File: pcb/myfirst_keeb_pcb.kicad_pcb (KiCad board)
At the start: 2 copper layers, 155 parts, among them SW1 SW_Push, SW2 SW_Push, SW3 Rotary_Encoder_Switch, U1 SRV05-4, U2 MCP1700-3302E_SOT23, U3 STM32F410CBTx

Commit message: remove switch for rst, use same switch as BOOT0 - add jtag for swd
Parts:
- removed SW2: SW_Push, Button_Switch_SMD:SW_SPST_B3S-1000
- added J1: Conn_ARM_JTAG_SWD_10, Connector_PinHeader_1.27mm:PinHeader_2x05_P1.27mm_Vertical_SMD, B.Cu at (157.4, 118.8)
- added Q1: DTC123J, Package_TO_SOT_SMD:SOT-23, B.Cu at (163.0, 128.0)
- moved C2 181.9 mm to (215.6, 125.7), turned to 90 degrees
- moved C6 96.4 mm to (200.5, 131.6)
- moved SW1 57.4 mm to (154.4, 128.0), turned to 180 degrees
- moved C7 39.3 mm to (198.6, 123.1), turned to 90 degrees
- moved C5 8.69 mm to (196.8, 128.5)
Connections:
- net Net-(R3-Pad2) renamed BOOT0
- C5 pad 2: GND -> NRST
- U3 pad 7: Net-(C5-Pad1) -> NRST
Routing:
- net SWDIO: track 0.00 -> 78.7 mm, vias 0 -> 2
- net SWDCLK: track 0.00 -> 57.4 mm, vias 0 -> 2
- net NRST: track 0.00 -> 51.1 mm, vias 0 -> 4
- net BOOT0: track 13.6 -> 61.9 mm, vias 0 -> 2
- net Net-(C5-Pad1): track 55.8 -> 36.6 mm, vias 2 -> 0
- net GND: track 708.4 -> 698.1 mm, vias 3 -> 4
- net D+: track 505.8 -> 503.6 mm
- net D-: track 495.7 -> 493.6 mm
- net +3V3: track 395.9 -> 396.1 mm, vias 4 -> 6

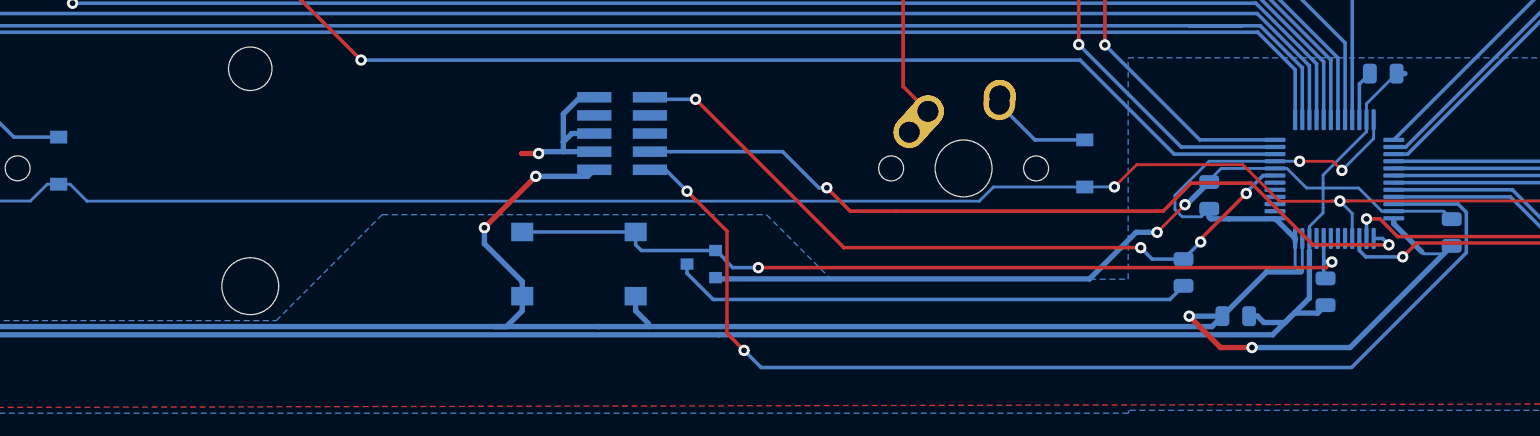
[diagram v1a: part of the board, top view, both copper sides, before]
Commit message: moved boot button to directly under spacebar
- easy push
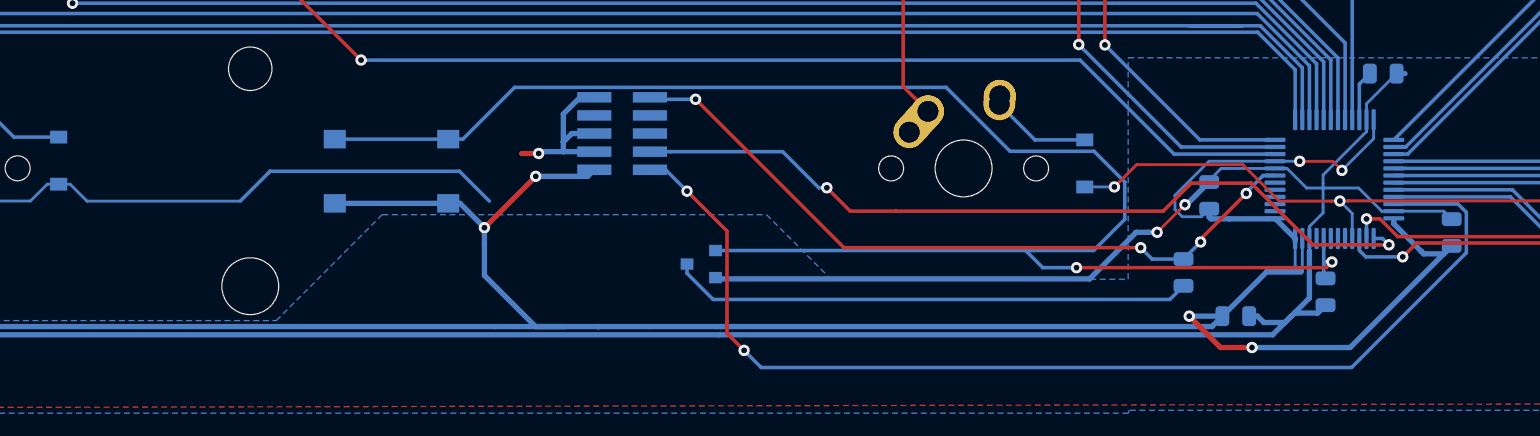
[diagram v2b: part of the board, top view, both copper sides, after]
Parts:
- moved SW1 14.7 mm to (141.3, 121.4)
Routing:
- net BOOT0: track 61.9 -> 117.4 mm
- net ROW4: track 313.8 -> 273.3 mm
- net +3V3: track 396.1 -> 406.4 mm

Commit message: shorten and made data bus lengths similar
- fix row trace unconnected
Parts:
- moved U1 7.50 mm to (116.7, 32.5)
- moved R2 6.98 mm to (111.1, 32.5)
- moved R1 6.12 mm to (111.1, 34.9)
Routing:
- net D+: track 503.6 -> 169.8 mm, vias 0 -> 7
- net D-: track 493.6 -> 169.8 mm, vias 0 -> 7
- net ROW4: track 273.3 -> 318.6 mm
- net GND: track 698.1 -> 705.4 mm
- net Net-(R2-Pad2): track 18.6 -> 11.9 mm
- net Net-(R1-Pad2): track 18.5 -> 12.2 mm
- net VCC: track 40.0 -> 38.5 mm

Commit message: add M2 mounting holes & rounded board cut-out
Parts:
- added H1: MountingHole, MountingHole:MountingHole_2.2mm_M2, F.Cu at (150.4, 31.1)
- added H2: MountingHole, MountingHole:MountingHole_2.2mm_M2, F.Cu at (255.1, 31.1)
- added H3: MountingHole, MountingHole:MountingHole_2.2mm_M2, F.Cu at (359.9, 31.1)
- added H4: MountingHole, MountingHole:MountingHole_2.2mm_M2, F.Cu at (359.9, 135.3)
- added H5: MountingHole, MountingHole:MountingHole_2.2mm_M2, F.Cu at (255.2, 135.3)
- added H6: MountingHole, MountingHole:MountingHole_2.2mm_M2, F.Cu at (150.4, 135.4)
- added H7: MountingHole, MountingHole:MountingHole_2.2mm_M2, F.Cu at (45.6, 135.3)
- added H8: MountingHole, MountingHole:MountingHole_2.2mm_M2, F.Cu at (45.6, 31.1)
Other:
- board outline added: 320.9 x 111.1 mm
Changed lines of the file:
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@@
   (general
     (thickness 1.6)
-    (drawings 2000)
+    (drawings 2008)
     (tracks 1199)
     (zones 0)
-    (modules 156)
+    (modules 164)
     (nets 122)
   )
@@
     (add_net VCC)
   )
+  (module MountingHole:MountingHole_2.2mm_M2 (layer F.Cu)
+    (at 45.62 31.11)
+    (descr "Mounting Hole 2.2mm, no annular, M2")
+    (tags "mounting hole 2.2mm no annular m2")
+    (attr virtual)
+    (fp_text reference H8 (at 0 -3.2) (layer F.SilkS)
+      (effects (font (size 1 1) (thickness 0.15)))
+    )
+    (fp_text value MountingHole (at 0 3.2) (layer F.Fab)
+      (effects (font (size 1 1) (thickness 0.15)))
+    )
+    (fp_text user %R (at 0.3 0) (layer F.Fab)
+      (effects (font (size 1 1) (thickness 0.15)))
+    )
+    (fp_circle (center 0 0) (end 2.2 0) (layer Cmts.User) (width 0.15))
+    (fp_circle (center 0 0) (end 2.45 0) (layer F.CrtYd) (width 0.05))
+    (pad 1 np_thru_hole circle (at 0 0) (size 2.2 2.2) (drill 2.2) (layers *.Cu *.Mask))
+  )
+  (module MountingHole:MountingHole_2.2mm_M2 (layer F.Cu)
+    (at 45.6 135.35)
+    (descr "Mounting Hole 2.2mm, no annular, M2")
+    (tags "mounting hole 2.2mm no annular m2")
+    (attr virtual)
+    (fp_text reference H7 (at 0 -3.2) (layer F.SilkS)
+      (effects (font (size 1 1) (thickness 0.15)))
+    )
+    (fp_text value MountingHole (at 0 3.2) (layer F.Fab)
+      (effects (font (size 1 1) (thickness 0.15)))
+    )
+    (fp_circle (center 0 0) (end 2.45 0) (layer F.CrtYd) (width 0.05))
+    (fp_circle (center 0 0) (end 2.2 0) (layer Cmts.User) (width 0.15))
+    (fp_text user %R (at 0.3 0) (layer F.Fab)
+      (effects (font (size 1 1) (thickness 0.15)))
+    )
+    (pad 1 np_thru_hole circle (at 0 0) (size 2.2 2.2) (drill 2.2) (layers *.Cu *.Mask))
+  )
+  (module MountingHole:MountingHole_2.2mm_M2 (layer F.Cu)
+    (at 150.37 135.36)
+    (descr "Mounting Hole 2.2mm, no annular, M2")
+    (tags "mounting hole 2.2mm no annular m2")
+    (attr virtual)
+    (fp_text reference H6 (at 0 -3.2) (layer F.SilkS)
+      (effects (font (size 1 1) (thickness 0.15)))
+    )
+    (fp_text value MountingHole (at 0 3.2) (layer F.Fab)
+      (effects (font (size 1 1) (thickness 0.15)))
+    )
+    (fp_circle (center 0 0) (end 2.45 0) (layer F.CrtYd) (width 0.05))
+    (fp_circle (center 0 0) (end 2.2 0) (layer Cmts.User) (width 0.15))
+    (fp_text user %R (at 0.3 0) (layer F.Fab)
+      (effects (font (size 1 1) (thickness 0.15)))
+    )
+    (pad 1 np_thru_hole circle (at 0 0) (size 2.2 2.2) (drill 2.2) (layers *.Cu *.Mask))
+  )
+  (module MountingHole:MountingHole_2.2mm_M2 (layer F.Cu)
+    (at 255.15 135.33)
+    (descr "Mounting Hole 2.2mm, no annular, M2")
+    (tags "mounting hole 2.2mm no annular m2")
+    (attr virtual)
+    (fp_text reference H5 (at 0 -3.2) (layer F.SilkS)
+      (effects (font (size 1 1) (thickness 0.15)))
+    )
+    (fp_text value MountingHole (at 0 3.2) (layer F.Fab)
+      (effects (font (size 1 1) (thickness 0.15)))
+    )
+    (fp_circle (center 0 0) (end 2.45 0) (layer F.CrtYd) (width 0.05))
+    (fp_circle (center 0 0) (end 2.2 0) (layer Cmts.User) (width 0.15))
+    (fp_text user %R (at 0.3 0) (layer F.Fab)
+      (effects (font (size 1 1) (thickness 0.15)))
+    )
+    (pad 1 np_thru_hole circle (at 0 0) (size 2.2 2.2) (drill 2.2) (layers *.Cu *.Mask))
+  )
+  (module MountingHole:MountingHole_2.2mm_M2 (layer F.Cu)
+    (at 359.91 135.35)
+    (descr "Mounting Hole 2.2mm, no annular, M2")
+    (tags "mounting hole 2.2mm no annular m2")
+    (attr virtual)
+    (fp_text reference H4 (at 0 -3.2) (layer F.SilkS)
+      (effects (font (size 1 1) (thickness 0.15)))
+    )
+    (fp_text value MountingHole (at 0 3.2) (layer F.Fab)
+      (effects (font (size 1 1) (thickness 0.15)))
+    )
+    (fp_circle (center 0 0) (end 2.45 0) (layer F.CrtYd) (width 0.05))
+    (fp_circle (center 0 0) (end 2.2 0) (layer Cmts.User) (width 0.15))
+    (fp_text user %R (at 0.3 0) (layer F.Fab)
+      (effects (font (size 1 1) (thickness 0.15)))
+    )
+    (pad 1 np_thru_hole circle (at 0 0) (size 2.2 2.2) (drill 2.2) (layers *.Cu *.Mask))
+  )
+  (module MountingHole:MountingHole_2.2mm_M2 (layer F.Cu)
+    (at 359.91 31.1)
+    (descr "Mounting Hole 2.2mm, no annular, M2")
+    (tags "mounting hole 2.2mm no annular m2")
+    (attr virtual)
+    (fp_text reference H3 (at 0 -3.2) (layer F.SilkS)
+      (effects (font (size 1 1) (thickness 0.15)))
+    )
+    (fp_text value MountingHole (at 0 3.2) (layer F.Fab)
+      (effects (font (size 1 1) (thickness 0.15)))
+    )
+    (fp_circle (center 0 0) (end 2.45 0) (layer F.CrtYd) (width 0.05))
+    (fp_circle (center 0 0) (end 2.2 0) (layer Cmts.User) (width 0.15))
+    (fp_text user %R (at 0.3 0) (layer F.Fab)
+      (effects (font (size 1 1) (thickness 0.15)))
+    )
+    (pad 1 np_thru_hole circle (at 0 0) (size 2.2 2.2) (drill 2.2) (layers *.Cu *.Mask))
+  )
+  (module MountingHole:MountingHole_2.2mm_M2 (layer F.Cu)
+    (at 255.14 31.1)
+    (descr "Mounting Hole 2.2mm, no annular, M2")
+    (tags "mounting hole 2.2mm no annular m2")
+    (attr virtual)
+    (fp_text reference H2 (at 0 -3.2) (layer F.SilkS)
+      (effects (font (size 1 1) (thickness 0.15)))
+    )
+    (fp_text value MountingHole (at 0 3.2) (layer F.Fab)
+      (effects (font (size 1 1) (thickness 0.15)))
+    )
+    (fp_circle (center 0 0) (end 2.45 0) (layer F.CrtYd) (width 0.05))
+    (fp_circle (center 0 0) (end 2.2 0) (layer Cmts.User) (width 0.15))
+    (fp_text user %R (at 0.3 0) (layer F.Fab)
+      (effects (font (size 1 1) (thickness 0.15)))
+    )
+    (pad 1 np_thru_hole circle (at 0 0) (size 2.2 2.2) (drill 2.2) (layers *.Cu *.Mask))
+  )
+  (module MountingHole:MountingHole_2.2mm_M2 (layer F.Cu)
+    (at 150.4 31.115)
+    (descr "Mounting Hole 2.2mm, no annular, M2")
+    (tags "mounting hole 2.2mm no annular m2")
+    (attr virtual)
+    (fp_text reference H1 (at 0 -3.2) (layer F.SilkS)
+      (effects (font (size 1 1) (thickness 0.15)))
+    )
+    (fp_text value MountingHole (at 0 3.2) (layer F.Fab)
+      (effects (font (size 1 1) (thickness 0.15)))
+    )
+    (fp_circle (center 0 0) (end 2.45 0) (layer F.CrtYd) (width 0.05))
+    (fp_circle (center 0 0) (end 2.2 0) (layer Cmts.User) (width 0.15))
+    (fp_text user %R (at 0.3 0) (layer F.Fab)
+      (effects (font (size 1 1) (thickness 0.15)))
+    )
+    (pad 1 np_thru_hole circle (at 0 0) (size 2.2 2.2) (drill 2.2) (layers *.Cu *.Mask))
+  )
   (module MX_Alps_Hybrid:MX-6.25U-NoLED (layer F.Cu)
     (at 181.38648 121.24436)
@@
     )
   )
+  (gr_line (start 357.8 27.62) (end 47.69 27.62) (layer Edge.Cuts) (width 0.05))
+  (gr_line (start 363.18 133.375) (end 363.18 33) (layer Edge.Cuts) (width 0.05))
+  (gr_line (start 47.69 138.755) (end 357.8 138.755) (layer Edge.Cuts) (width 0.05))
+  (gr_line (start 42.31 33) (end 42.31 133.375) (layer Edge.Cuts) (width 0.05))
+  (gr_arc (start 357.8 133.375) (end 357.8 138.755) (angle -90) (layer Edge.Cuts) (width 0.05))
+  (gr_arc (start 357.8 33) (end 363.18 33) (angle -90) (layer Edge.Cuts) (width 0.05))
+  (gr_arc (start 47.69 133.375) (end 42.31 133.375) (angle -90) (layer Edge.Cuts) (width 0.05))
+  (gr_arc (start 47.69 33) (end 47.69 27.62) (angle -90) (layer Edge.Cuts) (width 0.05))
   (gr_text Zap! (at 65.6 127.6) (layer F.SilkS)
     (effects (font (size 8 8) (thickness 1)))

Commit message: change microcontroller cause no stock
- shifted microcontroller position little bit nearer to usb
- fixed filling zones
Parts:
- C9: value 100nF -> 4.7uF
- U3: value STM32F410CBTx -> STM32F411RETx; footprint Package_QFP:LQFP-48_7x7mm_P0.5mm -> Package_QFP:LQFP-64_10x10mm_P0.5mm
- moved SW1 77.0 mm to (218.2, 121.5)
- moved C9 69.3 mm to (141.5, 113.2), turned to 90 degrees
- moved C6 61.2 mm to (139.8, 124.2)
- moved C2 60.7 mm to (154.9, 126.8), turned to 0 degrees
- moved U3 58.4 mm to (149.0, 120.0), turned to 90 degrees
- moved C7 44.2 mm to (155.6, 113.0), turned to 0 degrees
- moved J1 43.9 mm to (201.2, 121.5), turned to 90 degrees
- moved R3 36.7 mm to (170.5, 124.4)
- moved C5 32.8 mm to (164.0, 130.0), turned to 270 degrees
- moved Q1 5.47 mm to (167.2, 124.5)
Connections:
- net EXTRA_PIN_PB5 renamed Net-(U3-Pad41)
- net EXTRA_PIN_PB6 renamed Net-(U3-Pad42)
- net EXTRA_PIN_PB7 renamed Net-(U3-Pad43)
- U3 pad 10: ROW0 -> Net-(U3-Pad10)
- U3 pad 11: ROW1 -> Net-(U3-Pad11)
- U3 pad 12: ROW2 -> GND
- U3 pad 13: COL0 -> +3V3
- U3 pad 14: COL1 -> Net-(U3-Pad14)
- U3 pad 15: COL2 -> Net-(U3-Pad15)
- U3 pad 16: COL3 -> ROW4
- U3 pad 17: COL4 -> Net-(U3-Pad17)
- U3 pad 18: COL5 -> GND
- U3 pad 19: COL6 -> +3V3
- U3 pad 20: COL7 -> COL0
- U3 pad 21: COL8 -> COL1
- U3 pad 22: Net-(C9-Pad1) -> COL2
- U3 pad 23: GND -> COL3
- U3 pad 24: +3V3 -> ROW0
- U3 pad 25: ROW3 -> ROW1
- U3 pad 26: COL14 -> ROW2
- U3 pad 27: COL13 -> ROW3
- U3 pad 28: COL12 -> Net-(U3-Pad28)
- U3 pad 29: COL11 -> Net-(U3-Pad29)
- U3 pad 30: COL10 -> Net-(C9-Pad1)
- U3 pad 31: COL9 -> GND
- U3 pad 32: D- -> +3V3
- U3 pad 33: D+ -> COL4
- U3 pad 34: SWDIO -> COL5
- U3 pad 35: GND -> COL6
- U3 pad 36: +3V3 -> COL7
- U3 pad 37: SWDCLK -> COL8
- U3 pad 38: ENCODER_A -> COL9
- U3 pad 39: ENCODER_B -> COL10
- U3 pad 40: ROW4 -> Net-(U3-Pad40)
- U3 pad 44: BOOT0 -> D-
- U3 pad 45: EXTRA_PIN_PB8 -> D+
- U3 pad 46: GND -> SWDIO
- U3 pad 47: +3V3 -> GND
- U3 pad 8: GND -> Net-(U3-Pad8)
- U3 pad 9: +3V3 -> Net-(U3-Pad9)
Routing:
- net GND: track 705.4 -> 364.0 mm, vias 4 -> 7
- net COL4: track 146.4 -> 82.0 mm
- net COL1: track 206.3 -> 142.5 mm, vias 1 -> 3
- net COL9: track 128.6 -> 192.1 mm, vias 0 -> 1
- net COL3: track 166.4 -> 103.1 mm
- net D-: track 169.8 -> 106.7 mm, vias 7 -> 4
- net COL2: track 188.8 -> 125.7 mm
- net COL10: track 143.7 -> 206.1 mm
- net COL0: track 233.8 -> 172.6 mm, vias 0 -> 2
- net ROW0: track 603.6 -> 543.2 mm
- net COL11: track 131.1 -> 189.3 mm
- net COL12: track 172.0 -> 229.5 mm
- net D+: track 169.8 -> 112.5 mm, vias 7 -> 4
- net COL8: track 83.6 -> 140.1 mm
- net ENCODER_A: track 214.4 -> 269.0 mm
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
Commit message: move rc1 and rc2 to bottom side. adjust data line length to be similar. adjust filling zone dimensions
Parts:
- RC1, RC2: moved to B.Cu
- USB1: footprint Type-C:HRO-TYPE-C-31-M-12 -> Type-C:HRO-TYPE-C-31-M-12-Assembly
- moved RC2 10.2 mm to (95.0, 29.2), turned to 0 degrees
- moved RC1 5.61 mm to (95.0, 31.2), turned to 0 degrees
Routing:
- net GND: track 364.0 -> 340.8 mm
- net Net-(RC2-Pad2): track 4.30 -> 14.2 mm, vias 1 -> 2
- net D-: track 106.7 -> 111.3 mm
- net Net-(RC1-Pad2): track 4.45 -> 8.73 mm, vias 1 -> 0
- net D+: track 112.5 -> 110.9 mm
